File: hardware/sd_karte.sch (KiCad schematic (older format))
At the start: 9 parts, among them CON1 SD_Card

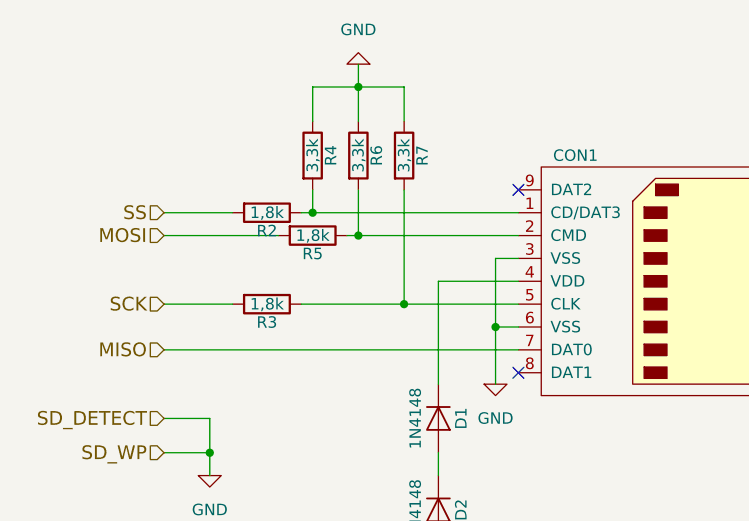
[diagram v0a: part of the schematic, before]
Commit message: Platine per Autorouter geroutet.
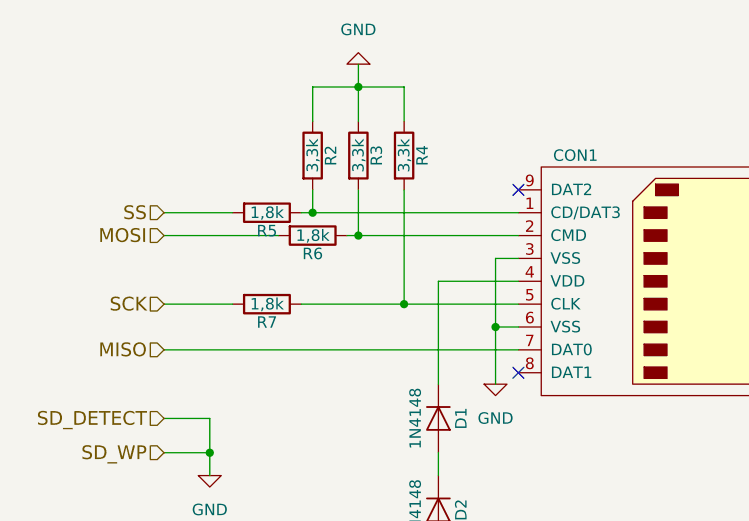
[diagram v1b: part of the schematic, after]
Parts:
- CON1: footprint Connect:SD_Card_Receptacle -> w_conn_misc:sd_socket
- renumbered R4 to R2, R6 to R3, R7 to R4, R2 to R5, R5 to R6, R3 to R7
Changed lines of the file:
@@
 LIBS:valves
 LIBS:Oscillators
+LIBS:w_analog
+LIBS:w_connectors
+LIBS:w_device
+LIBS:w_logic
+LIBS:w_memory
+LIBS:w_microcontrollers
+LIBS:w_opto
+LIBS:w_relay
+LIBS:w_rtx
+LIBS:w_transistor
+LIBS:w_vacuum
 LIBS:1541-rebuild-cache
 EELAYER 25 0
@@
 F 0 "CON1" H 6050 4250 50  0000 C CNN
 F 1 "SD_Card" H 7300 3150 50  0000 C CNN
-F 2 "Connect:SD_Card_Receptacle" H 6900 4050 50  0001 C CNN
+F 2 "w_conn_misc:sd_socket" H 6900 4050 50  0001 C CNN
 F 3 "" H 6700 3700 60  0000 C CNN
 	1    6700 3700
@@
 NoConn ~ 5800 3300
 $Comp
-L R R2
+L R R5
 U 1 1 55F7B36C
 P 4700 3400
-F 0 "R2" V 4780 3400 50  0000 C CNN
+F 0 "R5" V 4780 3400 50  0000 C CNN
 F 1 "1,8k" V 4700 3400 50  0000 C CNN
 F 2 "Resistors_ThroughHole:Resistor_Horizontal_RM10mm" V 4630 3400 30  0001 C CNN
@@
 $EndComp
 $Comp
-L R R5
+L R R6
 U 1 1 55F7B401
 P 4900 3500
-F 0 "R5" V 4980 3500 50  0000 C CNN
+F 0 "R6" V 4980 3500 50  0000 C CNN
 F 1 "1,8k" V 4900 3500 50  0000 C CNN
 F 2 "Resistors_ThroughHole:Resistor_Horizontal_RM10mm" V 4830 3500 30  0001 C CNN
@@
 $EndComp
 $Comp
-L R R3
+L R R7
 U 1 1 55F7B48C
 P 4700 3800
-F 0 "R3" V 4780 3800 50  0000 C CNN
+F 0 "R7" V 4780 3800 50  0000 C CNN
 F 1 "1,8k" V 4700 3800 50  0000 C CNN
 F 2 "Resistors_ThroughHole:Resistor_Horizontal_RM10mm" V 4630 3800 30  0001 C CNN
@@
 $EndComp
 $Comp
-L R R4
+L R R2
 U 1 1 55F7BA6C
 P 4900 3150
-F 0 "R4" V 4980 3150 50  0000 C CNN
+F 0 "R2" V 4980 3150 50  0000 C CNN
 F 1 "3,3k" V 4900 3150 50  0000 C CNN
 F 2 "Resistors_ThroughHole:Resistor_Horizontal_RM10mm" V 4830 3150 30  0001 C CNN
@@
 $EndComp
 $Comp
-L R R6
+L R R3
 U 1 1 55F7BC20
 P 5100 3150
-F 0 "R6" V 5180 3150 50  0000 C CNN
+F 0 "R3" V 5180 3150 50  0000 C CNN
 F 1 "3,3k" V 5100 3150 50  0000 C CNN
 F 2 "Resistors_ThroughHole:Resistor_Horizontal_RM10mm" V 5030 3150 30  0001 C CNN
@@
 $EndComp
 $Comp
-L R R7
+L R R4
 U 1 1 55F7BCCD
 P 5300 3150
-F 0 "R7" V 5380 3150 50  0000 C CNN
+F 0 "R4" V 5380 3150 50  0000 C CNN
 F 1 "3,3k" V 5300 3150 50  0000 C CNN
 F 2 "Resistors_ThroughHole:Resistor_Horizontal_RM10mm" V 5230 3150 30  0001 C CNN

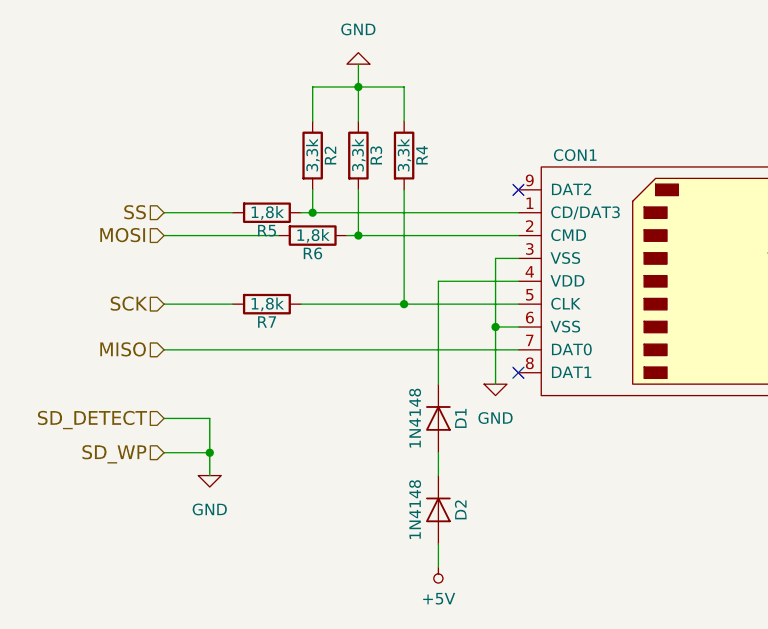
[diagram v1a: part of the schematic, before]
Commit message: Debug LED im Schaltplan eingefügt.
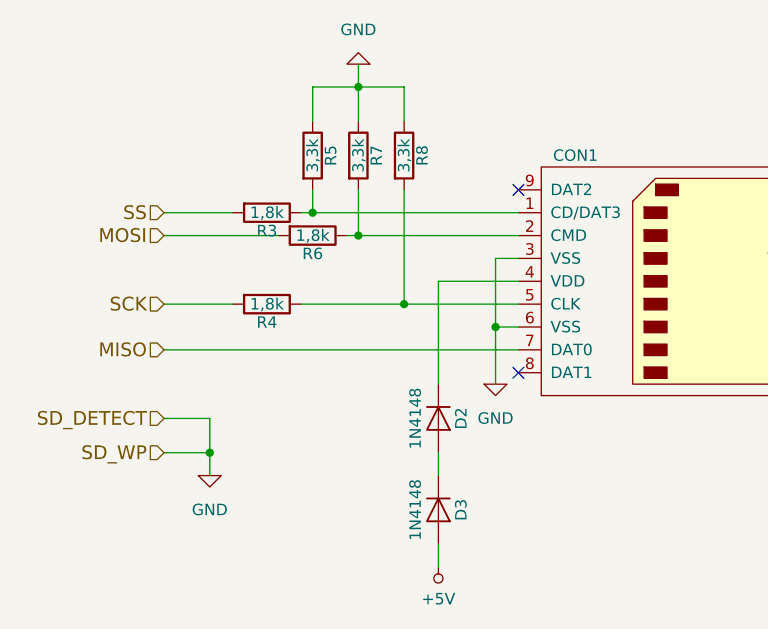
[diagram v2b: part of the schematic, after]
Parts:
- renumbered D1 to D2, D2 to D3, R5 to R3, R7 to R4, R2 to R5, R3 to R7, R4 to R8
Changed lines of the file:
@@
 Sheet 2 4
 Title "1541-rebuid"
-Date "2015-09-15"
-Rev "1.0"
+Date "2018-04-18"
+Rev "1.1"
 Comp ""
 Comment1 "Erstellt: von: Thorsten Kattanek"
@@
 $EndComp
 $Comp
-L GND #PWR011
+L GND #PWR15
 U 1 1 55F7A326
 P 5700 4150
-F 0 "#PWR011" H 5700 3900 50  0001 C CNN
+F 0 "#PWR15" H 5700 3900 50  0001 C CNN
 F 1 "GND" H 5700 4000 50  0000 C CNN
 F 2 "" H 5700 4150 60  0000 C CNN
@@
 $EndComp
 $Comp
-L D D1
+L D D2
 U 1 1 55F7A3CC
 P 5450 4300
-F 0 "D1" H 5450 4400 50  0000 C CNN
+F 0 "D2" H 5450 4400 50  0000 C CNN
 F 1 "1N4148" H 5450 4200 50  0000 C CNN
 F 2 "Diodes_ThroughHole:Diode_DO-35_SOD27_Horizontal_RM10" H 5450 4300 60  0001 C CNN
@@
 $EndComp
 $Comp
-L D D2
+L D D3
 U 1 1 55F7A4EB
 P 5450 4700
-F 0 "D2" H 5450 4800 50  0000 C CNN
+F 0 "D3" H 5450 4800 50  0000 C CNN
 F 1 "1N4148" H 5450 4600 50  0000 C CNN
 F 2 "Diodes_ThroughHole:Diode_DO-35_SOD27_Horizontal_RM10" H 5450 4700 60  0001 C CNN
@@
 $EndComp
 $Comp
-L +5V #PWR012
+L +5V #PWR14
 U 1 1 55F7A887
 P 5450 4950
-F 0 "#PWR012" H 5450 4800 50  0001 C CNN
+F 0 "#PWR14" H 5450 4800 50  0001 C CNN
 F 1 "+5V" H 5450 5090 50  0000 C CNN
 F 2 "" H 5450 4950 60  0000 C CNN
@@
 NoConn ~ 5800 3300
 $Comp
-L R R5
+L R R3
 U 1 1 55F7B36C
 P 4700 3400
-F 0 "R5" V 4780 3400 50  0000 C CNN
+F 0 "R3" V 4780 3400 50  0000 C CNN
 F 1 "1,8k" V 4700 3400 50  0000 C CNN
 F 2 "Resistors_ThroughHole:Resistor_Horizontal_RM10mm" V 4630 3400 30  0001 C CNN
@@
 $EndComp
 $Comp
-L R R7
+L R R4
 U 1 1 55F7B48C
 P 4700 3800
-F 0 "R7" V 4780 3800 50  0000 C CNN
+F 0 "R4" V 4780 3800 50  0000 C CNN
 F 1 "1,8k" V 4700 3800 50  0000 C CNN
 F 2 "Resistors_ThroughHole:Resistor_Horizontal_RM10mm" V 4630 3800 30  0001 C CNN
@@
 $EndComp
 $Comp
-L R R2
+L R R5
 U 1 1 55F7BA6C
 P 4900 3150
-F 0 "R2" V 4980 3150 50  0000 C CNN
+F 0 "R5" V 4980 3150 50  0000 C CNN
 F 1 "3,3k" V 4900 3150 50  0000 C CNN
 F 2 "Resistors_ThroughHole:Resistor_Horizontal_RM10mm" V 4830 3150 30  0001 C CNN
@@
 $EndComp
 $Comp
-L R R3
+L R R7
 U 1 1 55F7BC20
 P 5100 3150
-F 0 "R3" V 5180 3150 50  0000 C CNN
+F 0 "R7" V 5180 3150 50  0000 C CNN
 F 1 "3,3k" V 5100 3150 50  0000 C CNN
 F 2 "Resistors_ThroughHole:Resistor_Horizontal_RM10mm" V 5030 3150 30  0001 C CNN
@@
 $EndComp
 $Comp
-L R R4
+L R R8
 U 1 1 55F7BCCD
 P 5300 3150
-F 0 "R4" V 5380 3150 50  0000 C CNN
+F 0 "R8" V 5380 3150 50  0000 C CNN
 F 1 "3,3k" V 5300 3150 50  0000 C CNN
 F 2 "Resistors_ThroughHole:Resistor_Horizontal_RM10mm" V 5230 3150 30  0001 C CNN
@@
 $EndComp
 $Comp
-L GND #PWR013
+L GND #PWR13
 U 1 1 55F7BE30
 P 5100 2750
-F 0 "#PWR013" H 5100 2500 50  0001 C CNN
+F 0 "#PWR13" H 5100 2500 50  0001 C CNN
 F 1 "GND" H 5100 2600 50  0000 C CNN
 F 2 "" H 5100 2750 60  0000 C CNN
@@
 SD_WP
 $Comp
-L GND #PWR014
+L GND #PWR12
 U 1 1 583A74DE
 P 4450 4550
-F 0 "#PWR014" H 4450 4300 50  0001 C CNN
+F 0 "#PWR12" H 4450 4300 50  0001 C CNN
 F 1 "GND" H 4450 4400 50  0000 C CNN
 F 2 "" H 4450 4550 60  0000 C CNN

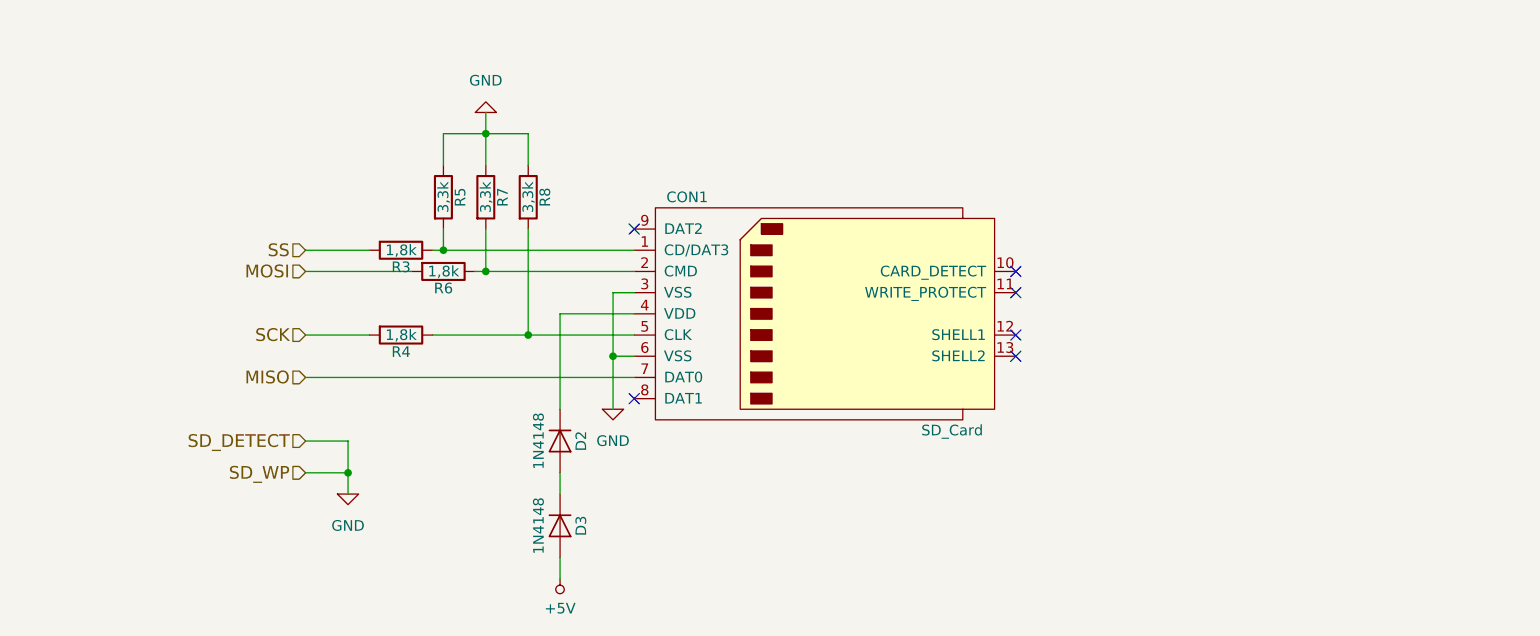
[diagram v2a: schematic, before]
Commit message: Änderungen am Schaltplan: - Resettaster eingefügt - SD Card Slot -> WP und DETECT richtig angeschlossen - auf Version 1.2 hochgesetzt
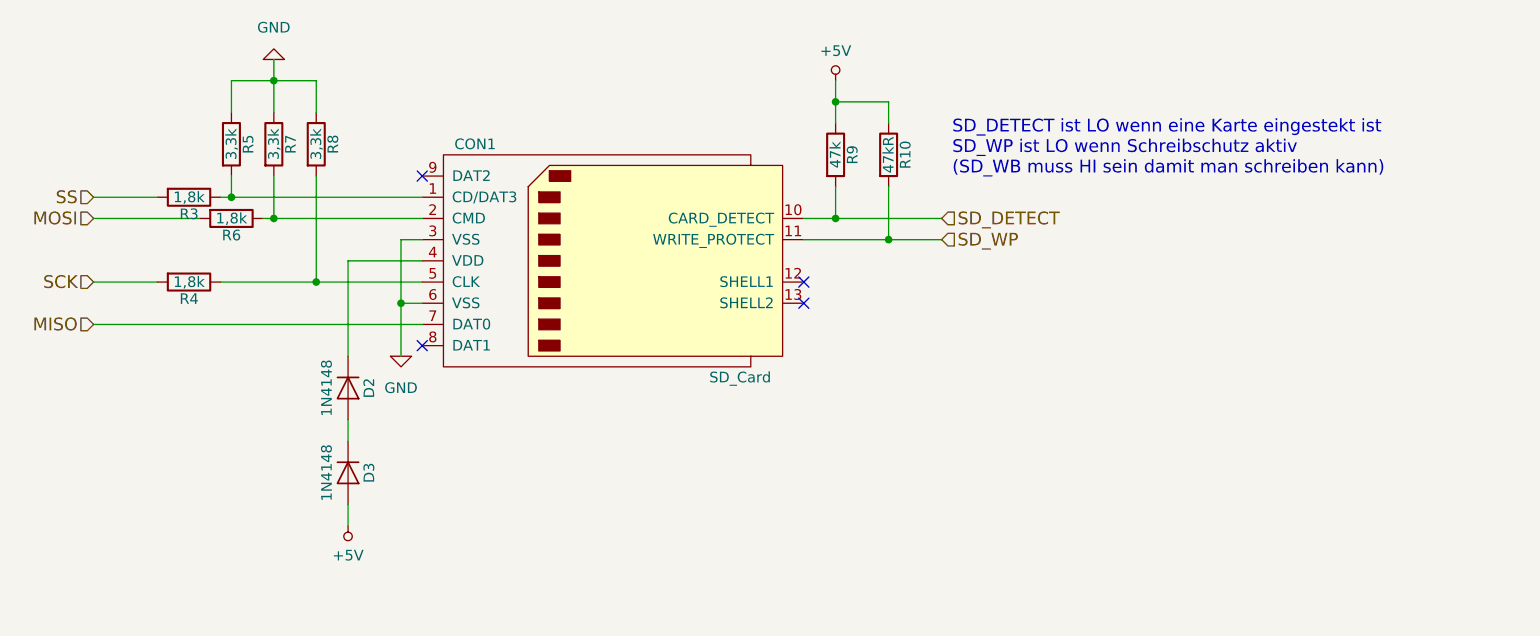
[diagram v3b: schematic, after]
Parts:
- added R10: 47kR, symbol R
- added R9: 47k, symbol R
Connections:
- net +5V: now also R10.1, R9.1
- net SD_DETECT: now reaches CON1.10 (CARD_DETECT)
- net SD_DETECT: now also R9.2
- net SD_WP: now reaches CON1.11 (WRITE_PROTECT)
- net SD_WP: now also R10.2
- no-connect marks 6 -> 4
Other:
- note added: "SD_DETECT ist LO wenn eine Karte eingestekt ist\nSD_WP ist LO wenn Schreibschutz aktiv\n(SD_WB muss HI sein damit man schreiben kann)"
- moved on the sheet: CON1, D2, D3, R3, R4, R5, R6, R7, R8

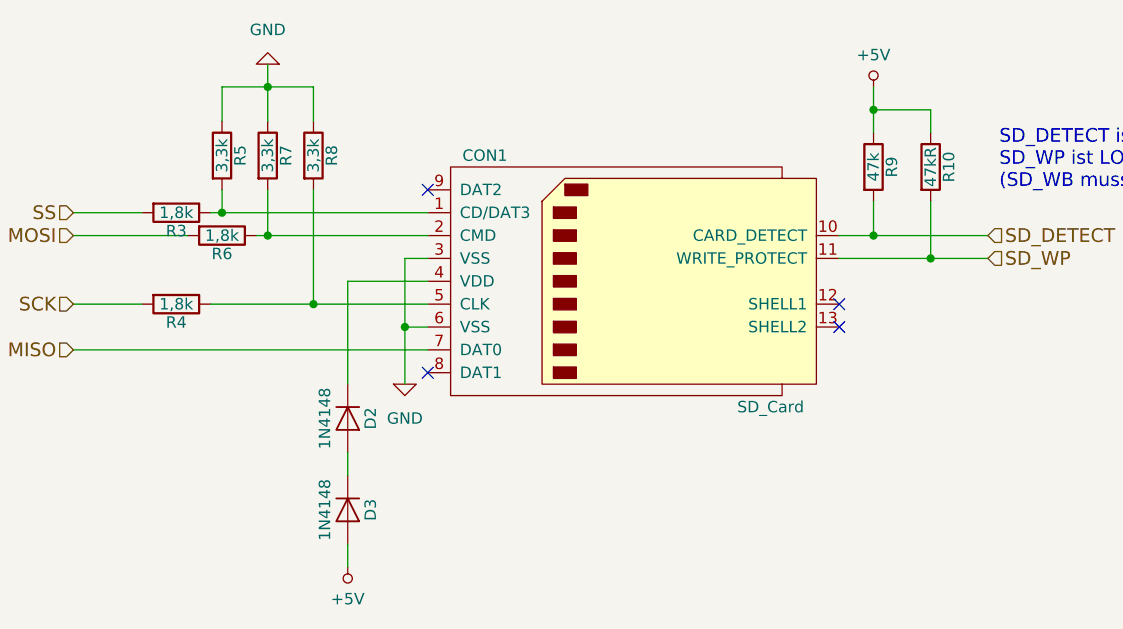
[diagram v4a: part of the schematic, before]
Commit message: Im Schaltplan die Debug LED mit Vorwiderstand durch einen PIN Header ersetz für eventuelle Erweiterung. Auf Revision 1.3 gesetzt
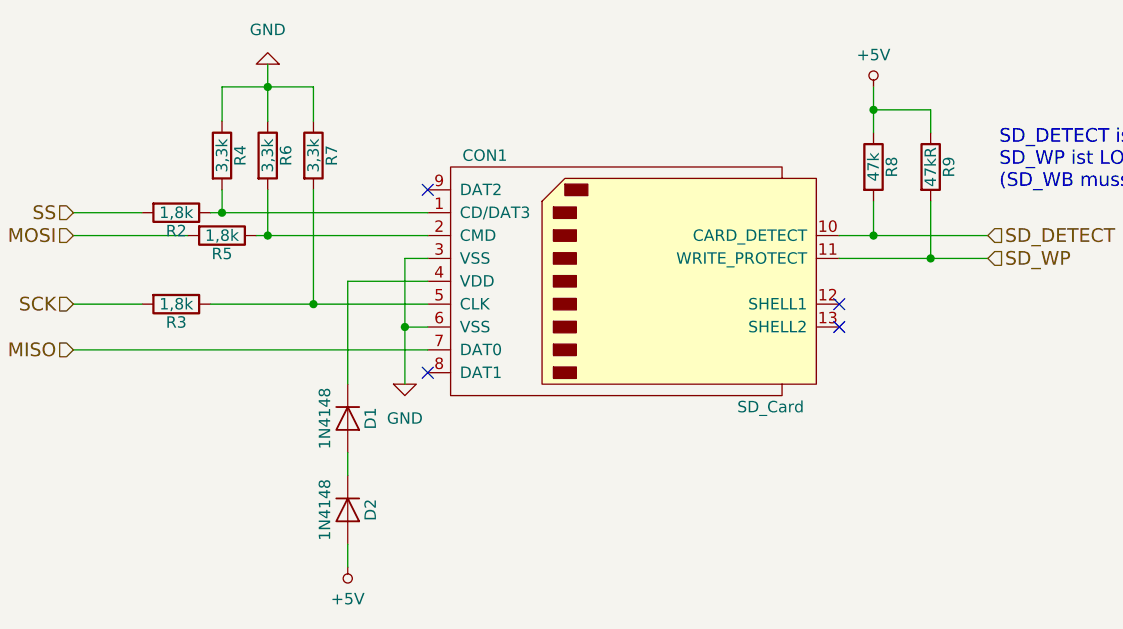
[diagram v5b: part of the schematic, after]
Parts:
- renumbered D2 to D1, D3 to D2, R3 to R2, R4 to R3, R5 to R4, R6 to R5, R7 to R6, R8 to R7, R9 to R8, R10 to R9
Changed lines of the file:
@@
 Sheet 2 4
 Title "1541-rebuid"
-Date "2018-05-04"
-Rev "1.2.1"
+Date "2018-05-05"
+Rev "1.3"
 Comp ""
 Comment1 "Erstellt: von: Thorsten Kattanek"
@@
 $EndComp
 $Comp
-L GND #PWR15
+L GND #PWR14
 U 1 1 55F7A326
 P 4700 3900
-F 0 "#PWR15" H 4700 3650 50  0001 C CNN
+F 0 "#PWR14" H 4700 3650 50  0001 C CNN
 F 1 "GND" H 4700 3750 50  0000 C CNN
 F 2 "" H 4700 3900 60  0000 C CNN
@@
 $EndComp
 $Comp
-L D D2
+L D D1
 U 1 1 55F7A3CC
 P 4450 4050
-F 0 "D2" H 4450 4150 50  0000 C CNN
+F 0 "D1" H 4450 4150 50  0000 C CNN
 F 1 "1N4148" H 4450 3950 50  0000 C CNN
 F 2 "Diodes_ThroughHole:Diode_DO-35_SOD27_Horizontal_RM10" H 4450 4050 60  0001 C CNN
@@
 $EndComp
 $Comp
-L D D3
+L D D2
 U 1 1 55F7A4EB
 P 4450 4450
-F 0 "D3" H 4450 4550 50  0000 C CNN
+F 0 "D2" H 4450 4550 50  0000 C CNN
 F 1 "1N4148" H 4450 4350 50  0000 C CNN
 F 2 "Diodes_ThroughHole:Diode_DO-35_SOD27_Horizontal_RM10" H 4450 4450 60  0001 C CNN
@@
 $EndComp
 $Comp
-L +5V #PWR14
+L +5V #PWR13
 U 1 1 55F7A887
 P 4450 4700
-F 0 "#PWR14" H 4450 4550 50  0001 C CNN
+F 0 "#PWR13" H 4450 4550 50  0001 C CNN
 F 1 "+5V" H 4450 4840 50  0000 C CNN
 F 2 "" H 4450 4700 60  0000 C CNN
@@
 NoConn ~ 4800 3050
 $Comp
-L R R3
+L R R2
 U 1 1 55F7B36C
 P 3700 3150
-F 0 "R3" V 3780 3150 50  0000 C CNN
+F 0 "R2" V 3780 3150 50  0000 C CNN
 F 1 "1,8k" V 3700 3150 50  0000 C CNN
 F 2 "Resistors_ThroughHole:Resistor_Horizontal_RM10mm" V 3630 3150 30  0001 C CNN
@@
 $EndComp
 $Comp
-L R R6
+L R R5
 U 1 1 55F7B401
 P 3900 3250
-F 0 "R6" V 3980 3250 50  0000 C CNN
+F 0 "R5" V 3980 3250 50  0000 C CNN
 F 1 "1,8k" V 3900 3250 50  0000 C CNN
 F 2 "Resistors_ThroughHole:Resistor_Horizontal_RM10mm" V 3830 3250 30  0001 C CNN
@@
 $EndComp
 $Comp
-L R R4
+L R R3
 U 1 1 55F7B48C
 P 3700 3550
-F 0 "R4" V 3780 3550 50  0000 C CNN
+F 0 "R3" V 3780 3550 50  0000 C CNN
 F 1 "1,8k" V 3700 3550 50  0000 C CNN
 F 2 "Resistors_ThroughHole:Resistor_Horizontal_RM10mm" V 3630 3550 30  0001 C CNN
@@
 $EndComp
 $Comp
-L R R5
+L R R4
 U 1 1 55F7BA6C
 P 3900 2900
-F 0 "R5" V 3980 2900 50  0000 C CNN
+F 0 "R4" V 3980 2900 50  0000 C CNN
 F 1 "3,3k" V 3900 2900 50  0000 C CNN
 F 2 "Resistors_ThroughHole:Resistor_Horizontal_RM10mm" V 3830 2900 30  0001 C CNN
@@
 $EndComp
 $Comp
-L R R7
+L R R6
 U 1 1 55F7BC20
 P 4100 2900
-F 0 "R7" V 4180 2900 50  0000 C CNN
+F 0 "R6" V 4180 2900 50  0000 C CNN
 F 1 "3,3k" V 4100 2900 50  0000 C CNN
 F 2 "Resistors_ThroughHole:Resistor_Horizontal_RM10mm" V 4030 2900 30  0001 C CNN
@@
 $EndComp
 $Comp
-L R R8
+L R R7
 U 1 1 55F7BCCD
 P 4300 2900
-F 0 "R8" V 4380 2900 50  0000 C CNN
+F 0 "R7" V 4380 2900 50  0000 C CNN
 F 1 "3,3k" V 4300 2900 50  0000 C CNN
 F 2 "Resistors_ThroughHole:Resistor_Horizontal_RM10mm" V 4230 2900 30  0001 C CNN
@@
 $EndComp
 $Comp
-L GND #PWR13
+L GND #PWR12
 U 1 1 55F7BE30
 P 4100 2500
-F 0 "#PWR13" H 4100 2250 50  0001 C CNN
+F 0 "#PWR12" H 4100 2250 50  0001 C CNN
 F 1 "GND" H 4100 2350 50  0000 C CNN
 F 2 "" H 4100 2500 60  0000 C CNN
@@
 Connection ~ 4700 3650
 $Comp
-L R R9
+L R R8
 U 1 1 5ADB73A5
 P 6750 2950
-F 0 "R9" V 6830 2950 50  0000 C CNN
+F 0 "R8" V 6830 2950 50  0000 C CNN
 F 1 "47k" V 6750 2950 50  0000 C CNN
 F 2 "" V 6680 2950 50  0001 C CNN
@@
 $EndComp
 $Comp
-L R R10
+L R R9
 U 1 1 5ADB753C
 P 7000 2950
-F 0 "R10" V 7080 2950 50  0000 C CNN
+F 0 "R9" V 7080 2950 50  0000 C CNN
 F 1 "47kR" V 7000 2950 50  0000 C CNN
 F 2 "" V 6930 2950 50  0001 C CNN
@@
 $EndComp
 $Comp
-L +5V #PWR16
+L +5V #PWR15
 U 1 1 5ADB75CA
 P 6750 2600
-F 0 "#PWR16" H 6750 2450 50  0001 C CNN
+F 0 "#PWR15" H 6750 2450 50  0001 C CNN
 F 1 "+5V" H 6750 2740 50  0000 C CNN
 F 2 "" H 6750 2600 60  0000 C CNN
